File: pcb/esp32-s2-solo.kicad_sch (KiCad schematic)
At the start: 8 parts, among them U1 ESP32-S2-SOLO

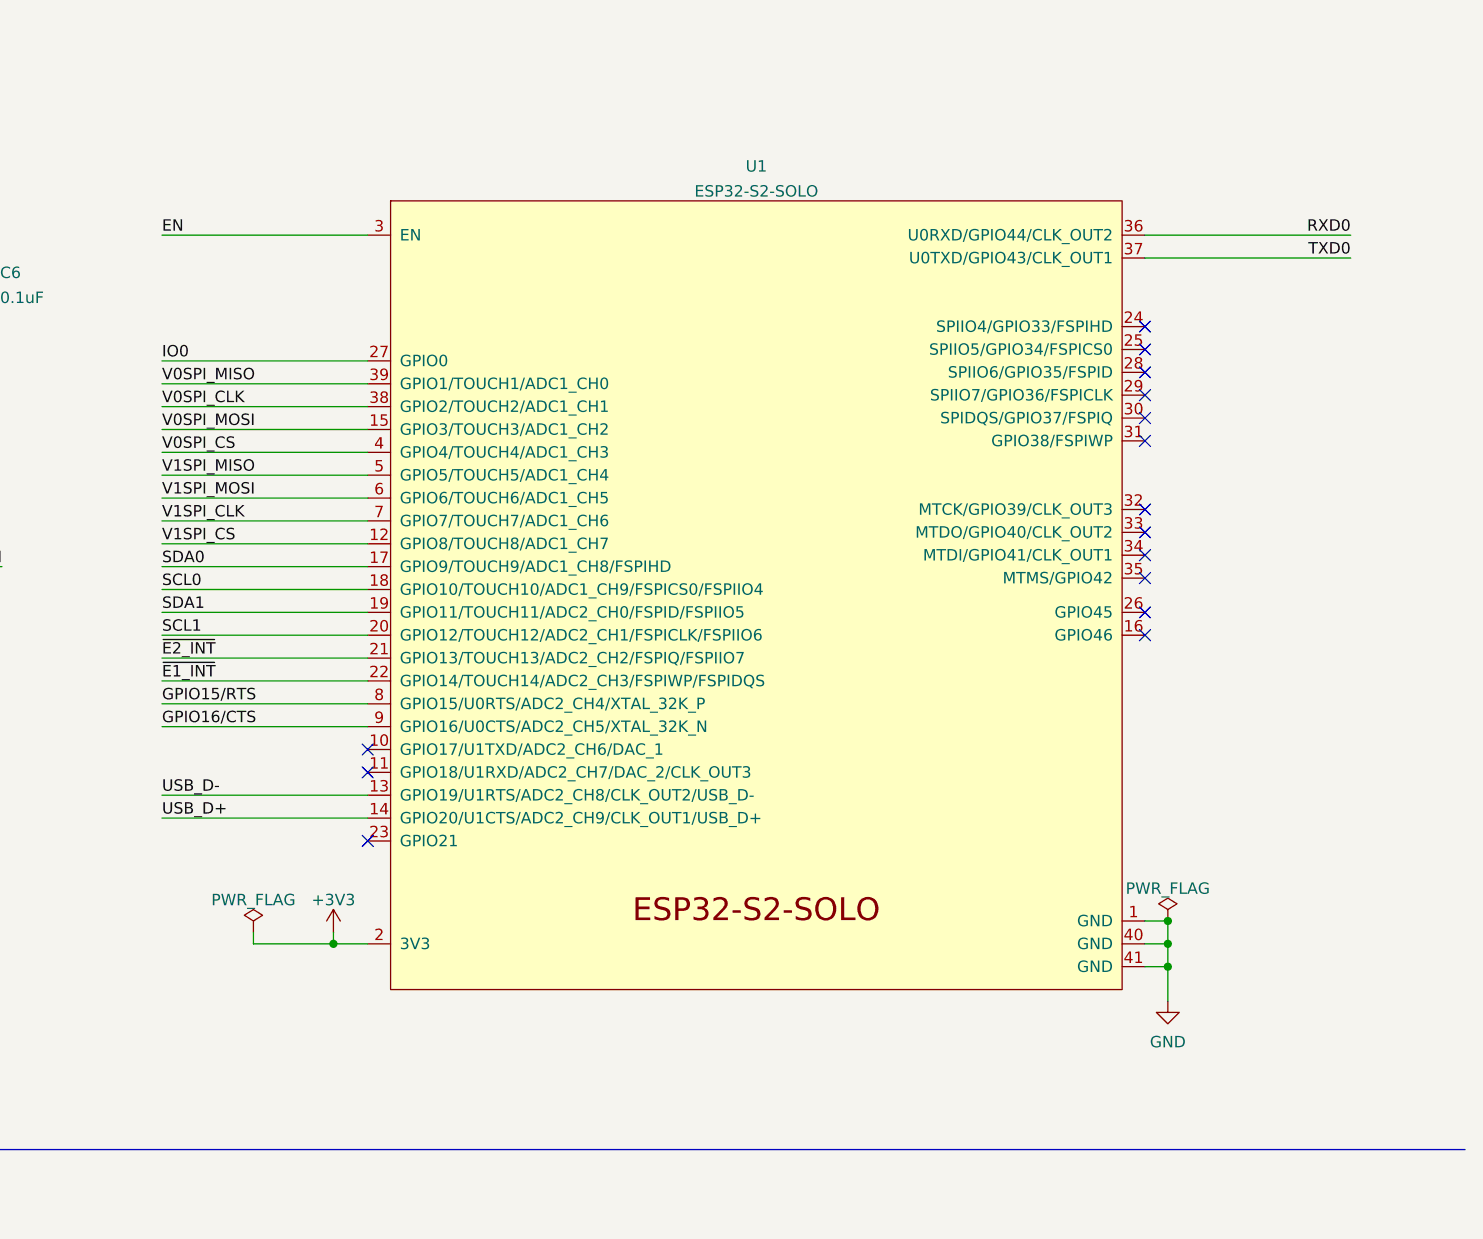
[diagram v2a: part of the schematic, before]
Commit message: Fix missing ESP-SOLO footprint and Symbol
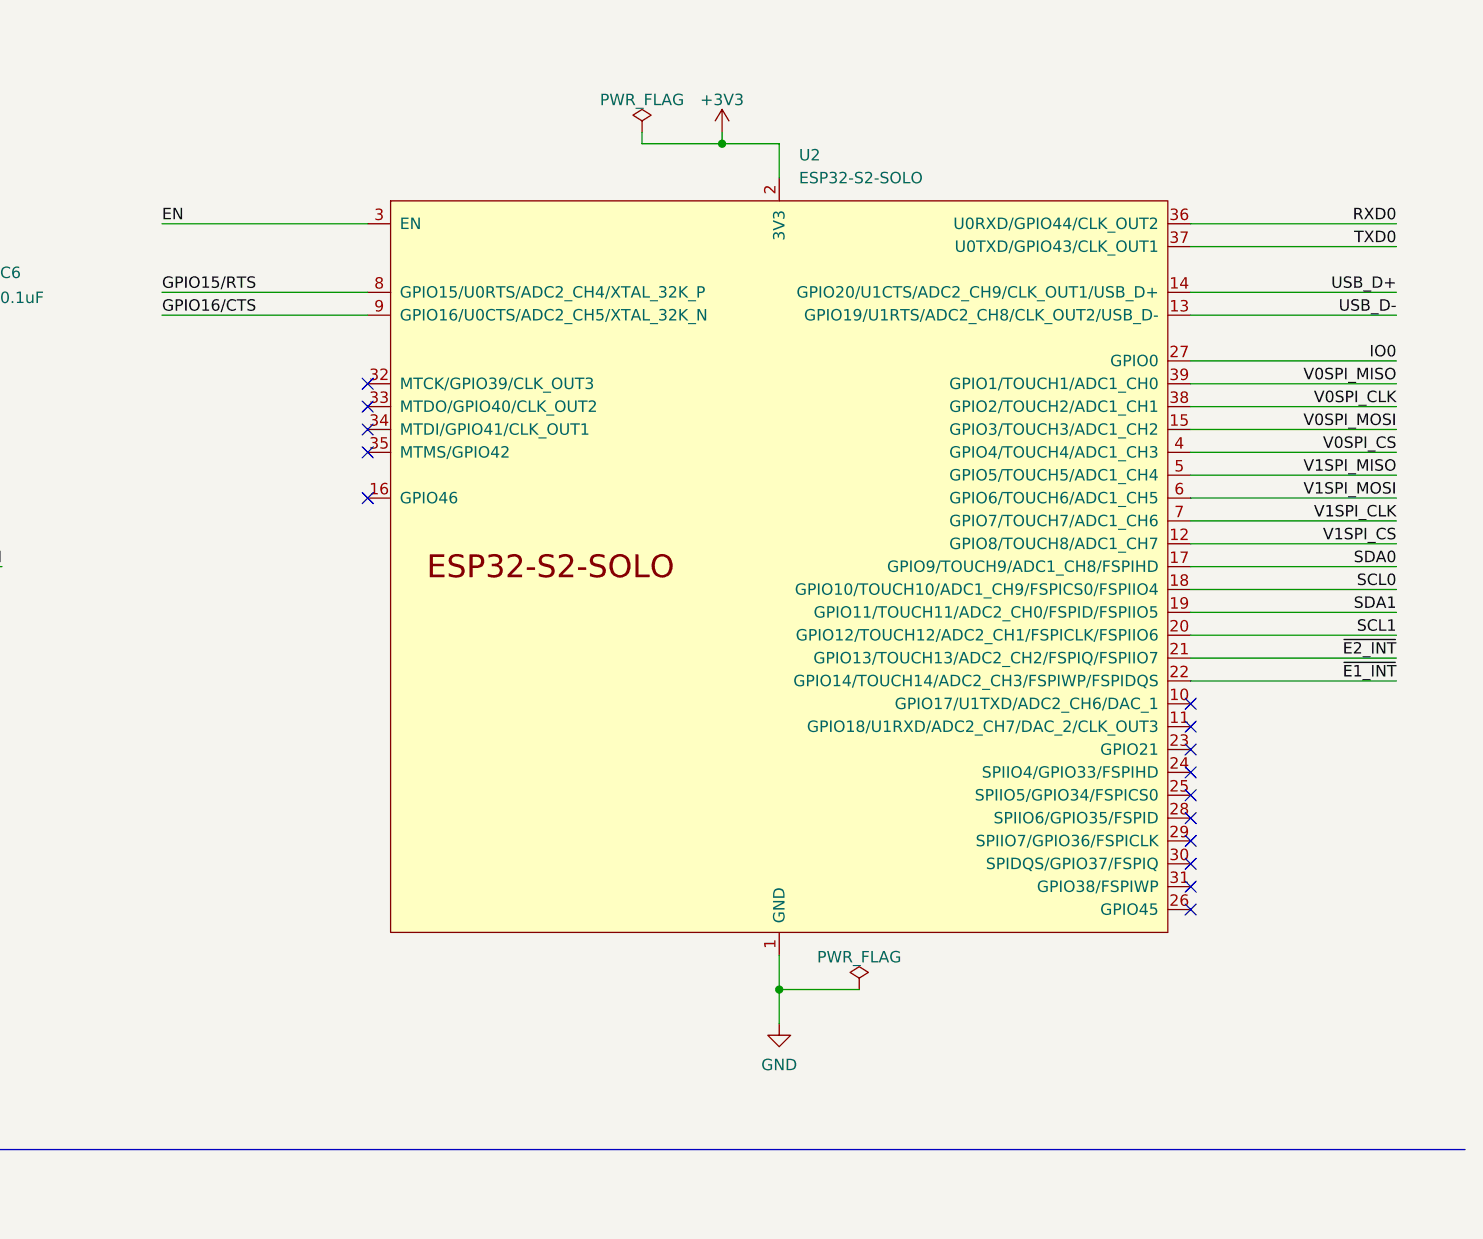
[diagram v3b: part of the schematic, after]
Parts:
- removed U1: ESP32-S2-SOLO, Espressif:ESP32-S2-SOLO, symbol Espressif:ESP32-S2-SOLO
- added U2: ESP32-S2-SOLO, PCM_Espressif:ESP32-S2-SOLO, symbol PCM_Espressif:ESP32-S2-SOLO
- S1: footprint KiCad:EVQPUA02K -> EVQ-PUA02K:EVQPUA02K
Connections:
- net +3V3: now also U2.2 (3V3)
- net ESP_EN/CM_RUN: now also U2.3 (EN)
- net GND: now also U2.1 (GND), U2.40 (GND), U2.41 (GND)
- net GPIO15/RTS: now also U2.8 (GPIO15/U0RTS/ADC2_CH4/XTAL_32K_P)
- net GPIO16/CTS: now also U2.9 (GPIO16/U0CTS/ADC2_CH5/XTAL_32K_N)
- net IO0: now also U2.27 (GPIO0)
- net RXD0: now also U2.36 (U0RXD/GPIO44/CLK_OUT2)
- net SCL0: now also U2.18 (GPIO10/TOUCH10/ADC1_CH9/FSPICS0/FSPIIO4)
- net SCL1: now also U2.20 (GPIO12/TOUCH12/ADC2_CH1/FSPICLK/FSPIIO6)
- net SDA0: now also U2.17 (GPIO9/TOUCH9/ADC1_CH8/FSPIHD)
- net SDA1: now also U2.19 (GPIO11/TOUCH11/ADC2_CH0/FSPID/FSPIIO5)
- net TXD0: now also U2.37 (U0TXD/GPIO43/CLK_OUT1)
- net USB_D+: now also U2.14 (GPIO20/U1CTS/ADC2_CH9/CLK_OUT1/USB_D+)
- net USB_D-: now also U2.13 (GPIO19/U1RTS/ADC2_CH8/CLK_OUT2/USB_D-)
- net V0SPI_CLK: now also U2.38 (GPIO2/TOUCH2/ADC1_CH1)
- net V0SPI_CS: now also U2.4 (GPIO4/TOUCH4/ADC1_CH3)
- net V0SPI_MISO: now also U2.39 (GPIO1/TOUCH1/ADC1_CH0)
- net V0SPI_MOSI: now also U2.15 (GPIO3/TOUCH3/ADC1_CH2)
- net V1SPI_CLK: now also U2.7 (GPIO7/TOUCH7/ADC1_CH6)
- net V1SPI_CS: now also U2.12 (GPIO8/TOUCH8/ADC1_CH7)
- net V1SPI_MISO: now also U2.5 (GPIO5/TOUCH5/ADC1_CH4)
- net V1SPI_MOSI: now also U2.6 (GPIO6/TOUCH6/ADC1_CH5)
- net ~{E1_INT}: now also U2.22 (GPIO14/TOUCH14/ADC2_CH3/FSPIWP/FSPIDQS)
- net ~{E2_INT}: now also U2.21 (GPIO13/TOUCH13/ADC2_CH2/FSPIQ/FSPIIO7)

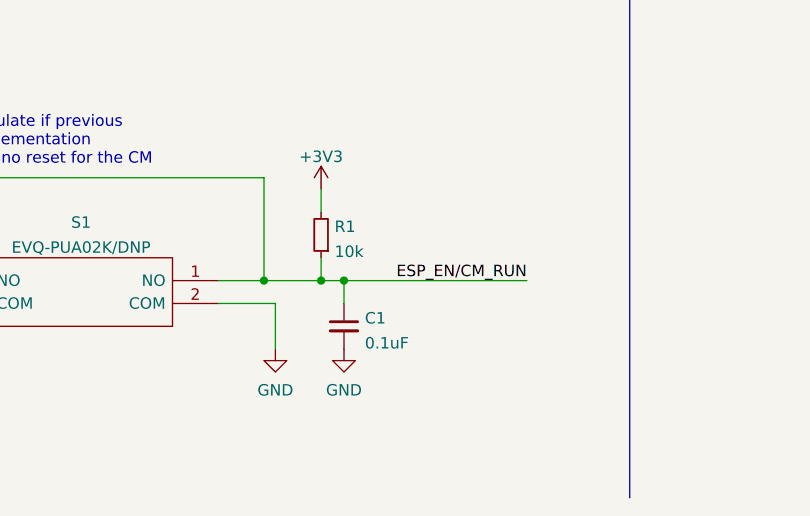
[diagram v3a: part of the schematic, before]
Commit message: Set reset button to be DNP
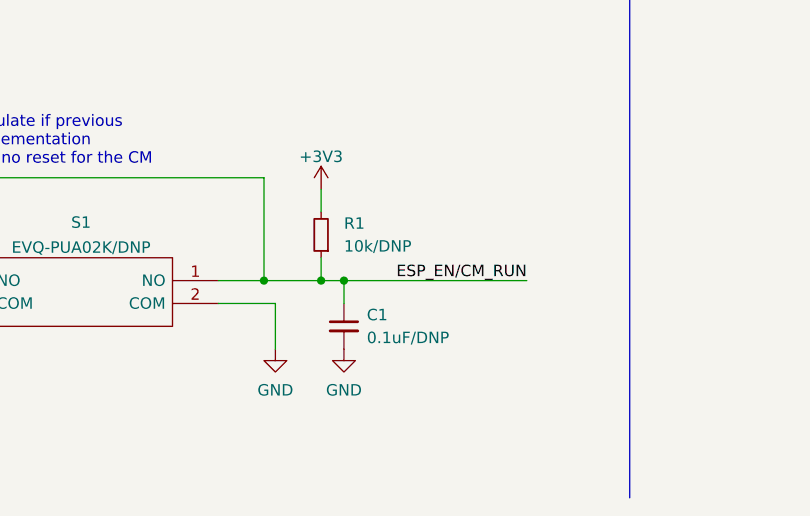
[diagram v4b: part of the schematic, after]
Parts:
- C1: value 0.1uF -> 0.1uF/DNP
- R1: value 10k -> 10k/DNP
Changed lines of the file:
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@@
   (symbol (lib_id "Device:R_Small") (at 74.93 167.64 180) (unit 1)
     (in_bom yes) (on_board yes) (dnp no) (fields_autoplaced)
-    (property "Reference" "R1" (at 76.4286 166.7315 0)
-      (effects (font (size 1.27 1.27)) (justify right))
-    )
-    (property "Value" "10k" (at 76.4286 169.5066 0)
+    (property "Reference" "R1" (at 77.47 166.37 0)
+      (effects (font (size 1.27 1.27)) (justify right))
+    )
+    (property "Value" "10k/DNP" (at 77.47 168.91 0)
       (effects (font (size 1.27 1.27)) (justify right))
     )
@@
   (symbol (lib_id "Device:C_Small") (at 77.47 177.8 0) (unit 1)
     (in_bom yes) (on_board yes) (dnp no) (fields_autoplaced)
-    (property "Reference" "C1" (at 79.7941 176.8978 0)
-      (effects (font (size 1.27 1.27)) (justify left))
-    )
-    (property "Value" "0.1uF" (at 79.7941 179.6729 0)
-      (effects (font (size 1.27 1.27)) (justify left))
-    )
+    (property "Reference" "C1" (at 80.01 176.5363 0)
+      (effects (font (size 1.27 1.27)) (justify left))
+    )
+    (property "Value" "0.1uF/DNP" (at 80.01 179.0763 0)
+      (effects (font (size 1.27 1.27)) (justify left))
+    )

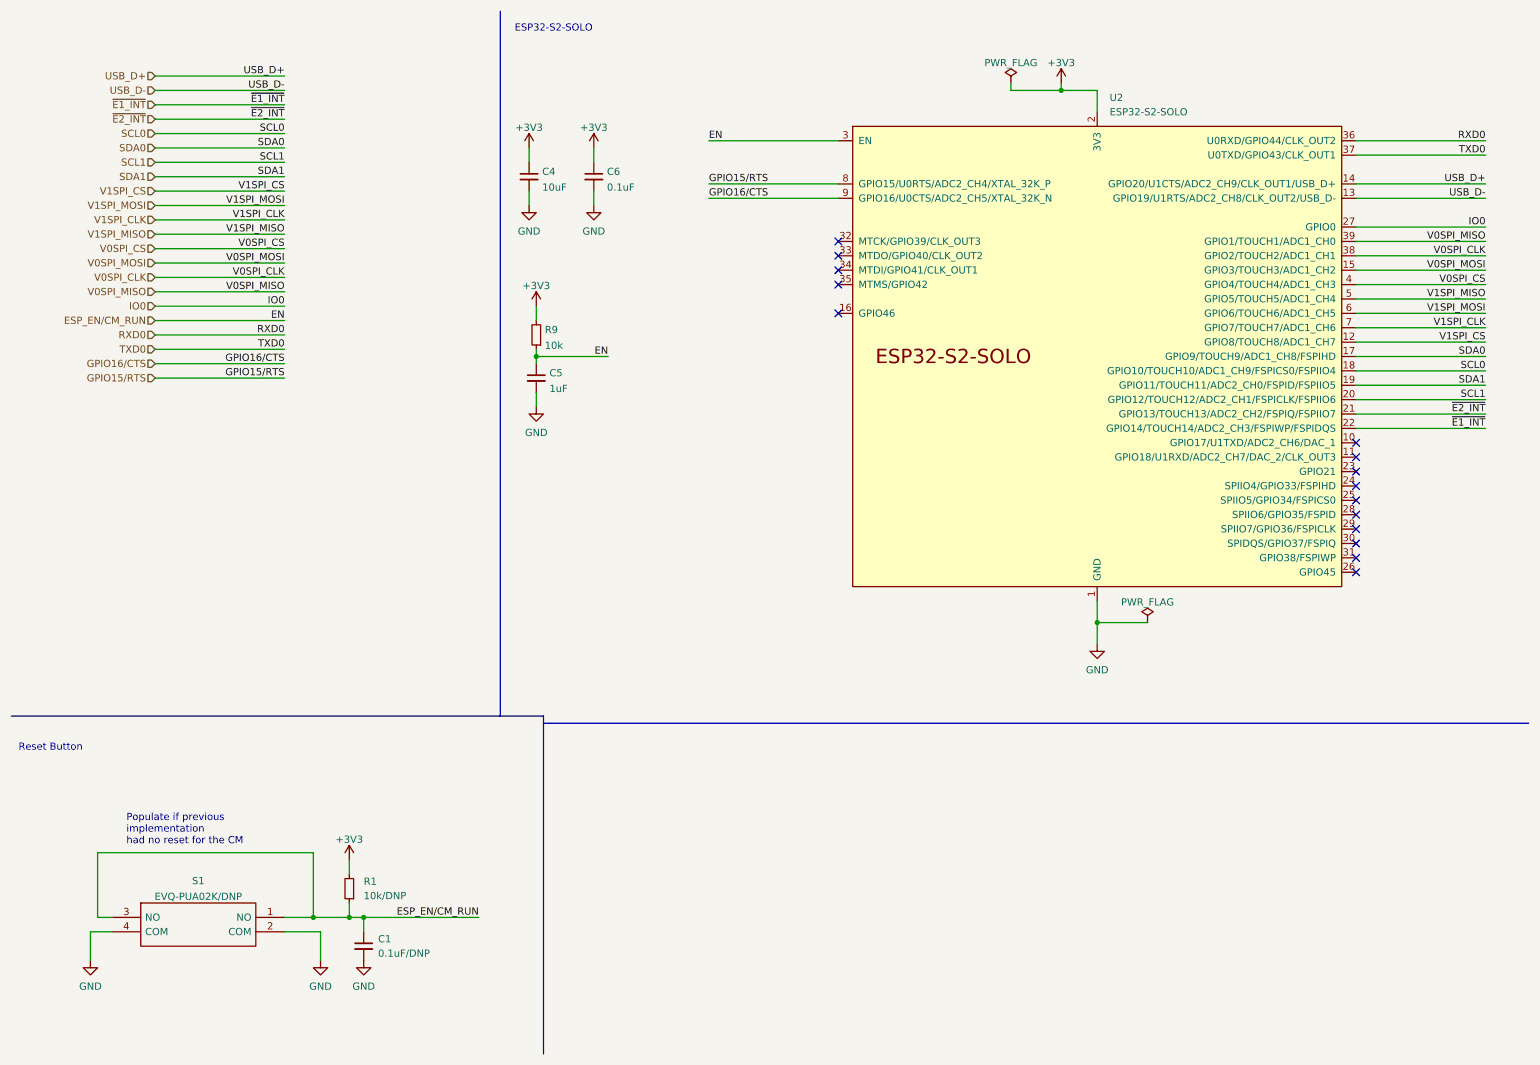
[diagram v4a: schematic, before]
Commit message: Removed parts from BOM and applied clearence changes
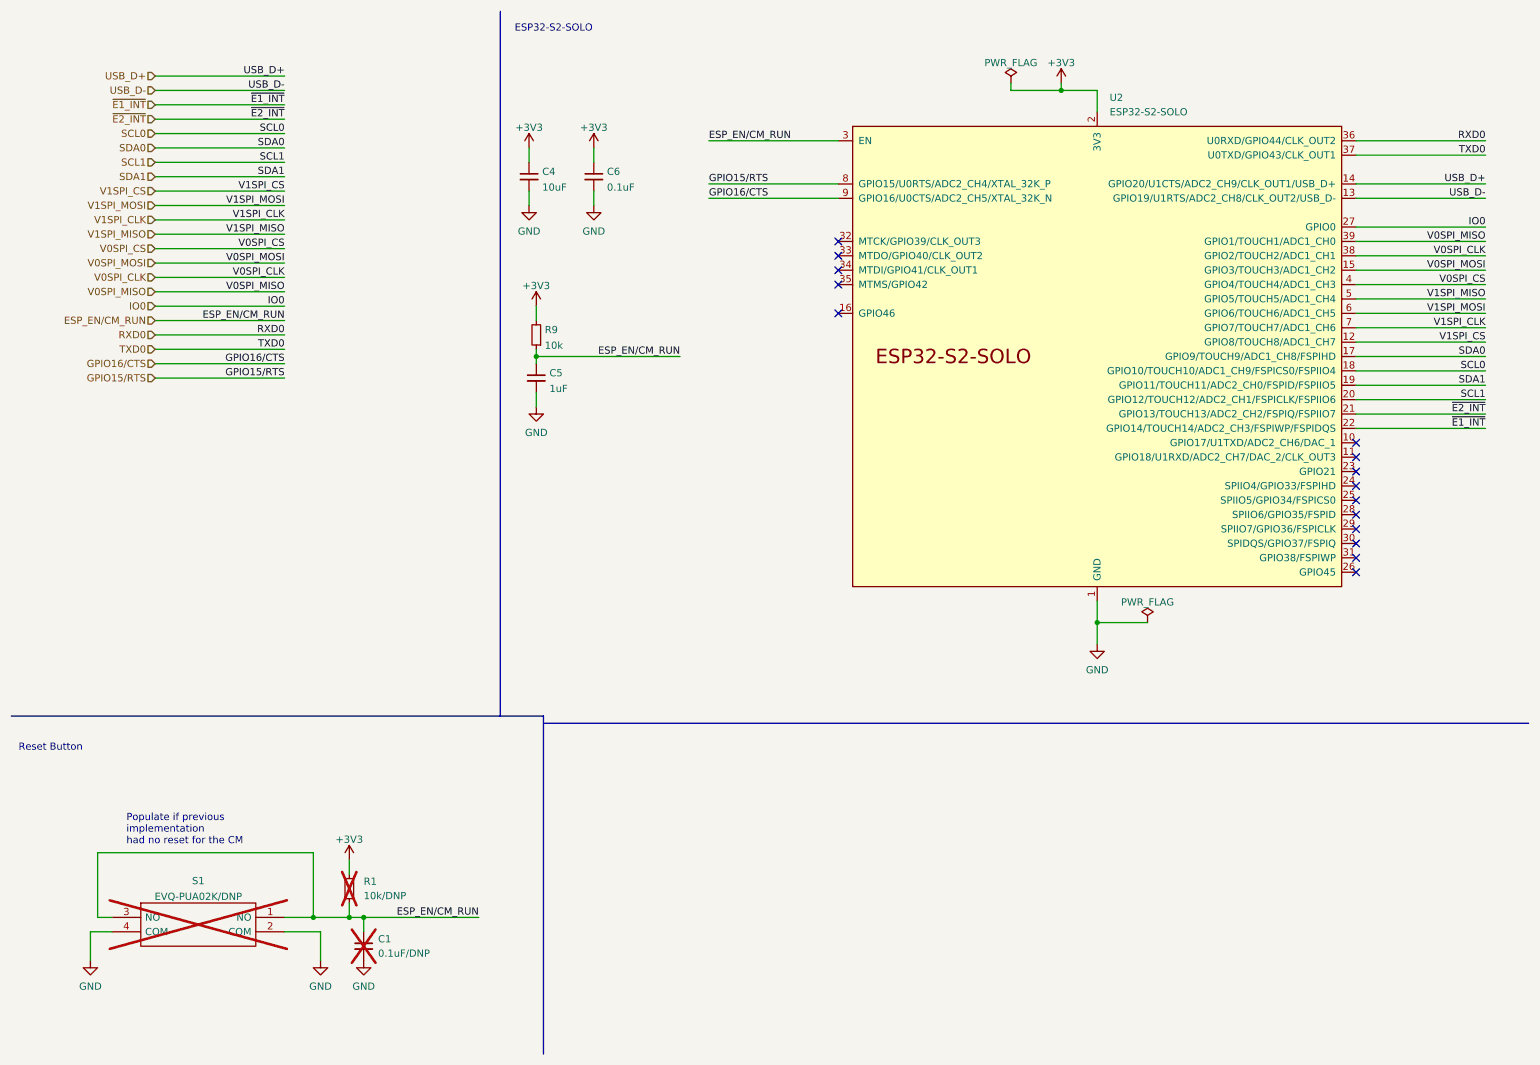
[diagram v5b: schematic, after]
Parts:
- C1, R1, S1: now not fitted; now left out of the parts list
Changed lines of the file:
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@@
     (stroke (width 0) (type default))
   )
-  (wire (pts (xy 107.95 73.66) (xy 120.65 73.66))
+  (wire (pts (xy 107.95 73.66) (xy 133.35 73.66))
     (stroke (width 0) (type default))
   )
@@
     (effects (font (size 1.27 1.27)) (justify left bottom))
   )
-  (label "EN" (at 138.43 35.56 0) (fields_autoplaced)
-    (effects (font (size 1.27 1.27)) (justify left bottom))
-  )
   (label "~{E1_INT}" (at 63.5 29.21 180) (fields_autoplaced)
     (effects (font (size 1.27 1.27)) (justify right bottom))
@@
     (effects (font (size 1.27 1.27)) (justify right bottom))
   )
-  (label "EN" (at 120.65 73.66 180) (fields_autoplaced)
-    (effects (font (size 1.27 1.27)) (justify right bottom))
-  )
   (label "GPIO15{slash}RTS" (at 63.5 77.47 180) (fields_autoplaced)
     (effects (font (size 1.27 1.27)) (justify right bottom))
@@
   )
   (label "V1SPI_CS" (at 63.5 44.45 180) (fields_autoplaced)
+    (effects (font (size 1.27 1.27)) (justify right bottom))
+  )
+  (label "ESP_EN{slash}CM_RUN" (at 133.35 73.66 180) (fields_autoplaced)
     (effects (font (size 1.27 1.27)) (justify right bottom))
   )
@@
     (effects (font (size 1.27 1.27)) (justify right bottom))
   )
+  (label "ESP_EN{slash}CM_RUN" (at 63.5 67.31 180) (fields_autoplaced)
+    (effects (font (size 1.27 1.27)) (justify right bottom))
+  )
   (label "V1SPI_MISO" (at 63.5 52.07 180) (fields_autoplaced)
     (effects (font (size 1.27 1.27)) (justify right bottom))
   )
-  (label "EN" (at 63.5 67.31 180) (fields_autoplaced)
-    (effects (font (size 1.27 1.27)) (justify right bottom))
-  )
   (label "V0SPI_MISO" (at 275.59 53.34 180) (fields_autoplaced)
     (effects (font (size 1.27 1.27)) (justify right bottom))
@@
   (label "V1SPI_CLK" (at 63.5 49.53 180) (fields_autoplaced)
     (effects (font (size 1.27 1.27)) (justify right bottom))
+  )
+  (label "ESP_EN{slash}CM_RUN" (at 138.43 35.56 0) (fields_autoplaced)
+    (effects (font (size 1.27 1.27)) (justify left bottom))
   )
   (label "GPIO15{slash}RTS" (at 138.43 43.18 0) (fields_autoplaced)
@@
   )
   (symbol (lib_id "Device:R_Small") (at 74.93 167.64 180) (unit 1)
-    (in_bom yes) (on_board yes) (dnp no) (fields_autoplaced)
+    (in_bom no) (on_board yes) (dnp yes) (fields_autoplaced)
     (property "Reference" "R1" (at 77.47 166.37 0)
       (effects (font (size 1.27 1.27)) (justify right))
@@
   )
   (symbol (lib_id "Device:C_Small") (at 77.47 177.8 0) (unit 1)
-    (in_bom yes) (on_board yes) (dnp no) (fields_autoplaced)
+    (in_bom no) (on_board yes) (dnp yes) (fields_autoplaced)
     (property "Reference" "C1" (at 80.01 176.5363 0)
       (effects (font (size 1.27 1.27)) (justify left))
@@
   )
   (symbol (lib_id "EVQ-PUA02K:EVQ-PUA02K") (at 33.02 172.72 0) (unit 1)
-    (in_bom yes) (on_board yes) (dnp no) (fields_autoplaced)
+    (in_bom no) (on_board yes) (dnp yes) (fields_autoplaced)
     (property "Reference" "S1" (at 48.26 166.2643 0)
       (effects (font (size 1.27 1.27)))
